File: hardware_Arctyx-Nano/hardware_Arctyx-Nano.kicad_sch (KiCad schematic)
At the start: 54 parts, among them J1 USB_C_Receptacle_USB2.0_16P, J2 Conn_01x20_Pin, J3 Conn_01x20_Pin, SW1 SW_Push, SW2 SW_Push, U1 ICE40UP5K-SG48ITR, U2 RP2350A-QFN60, U3 W25Q128JVS, U4 RT8075ZQW, U5 TJ-S1608SW6TDSLCCYRGB-A5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

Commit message: schematic
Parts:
- added D1, D2, D3, D4: LED, symbol Device:LED
- L2, L3: value L -> 3.3u
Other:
- moved on the sheet: J3

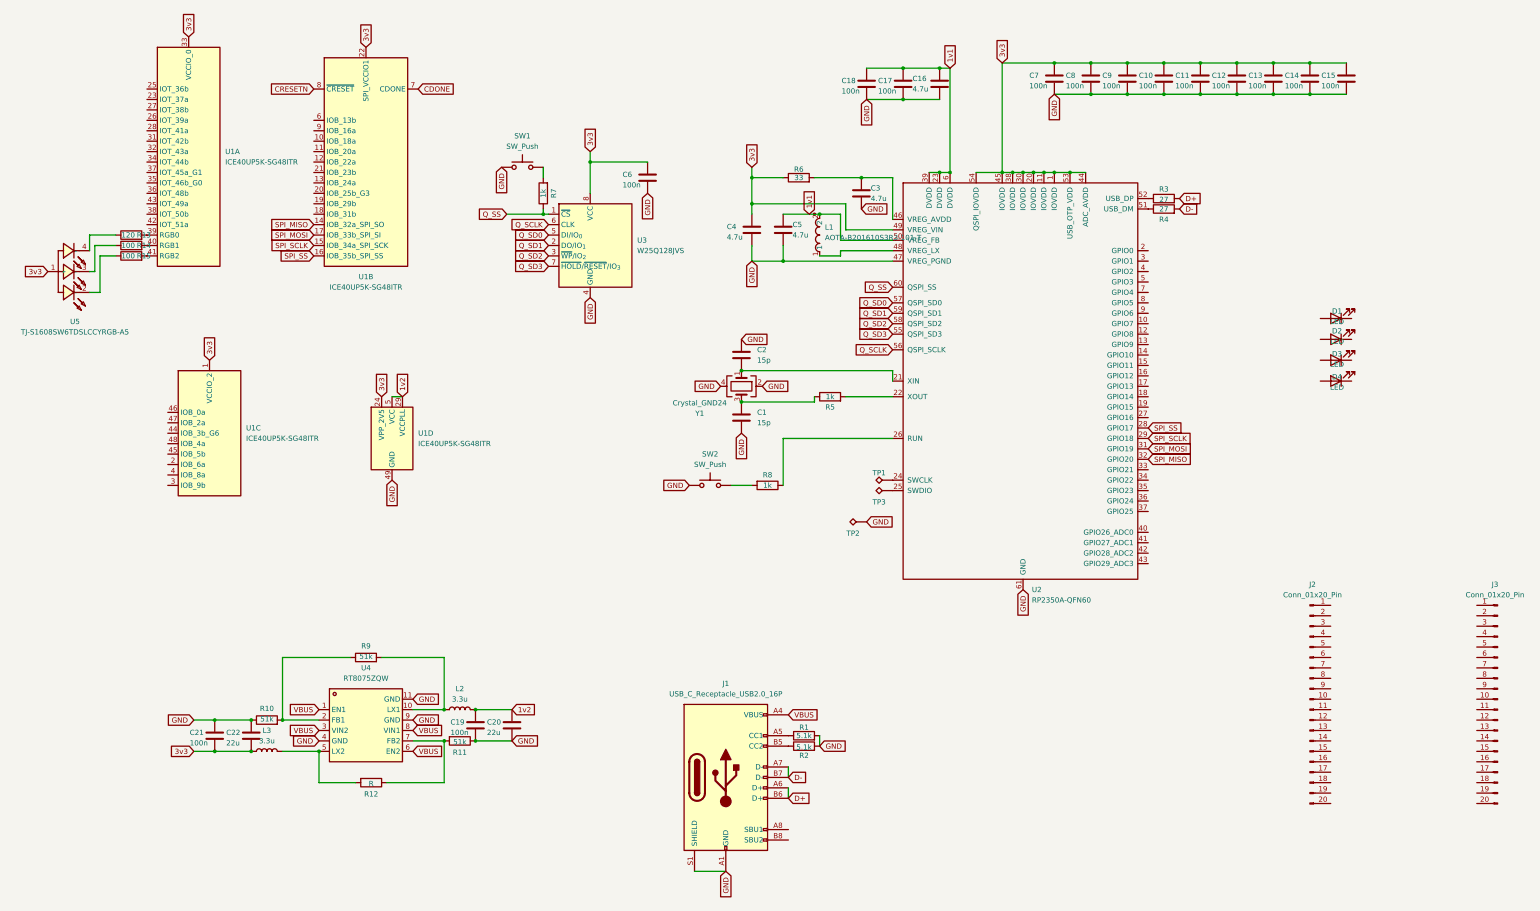
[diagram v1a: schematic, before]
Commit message: Routing the PCB
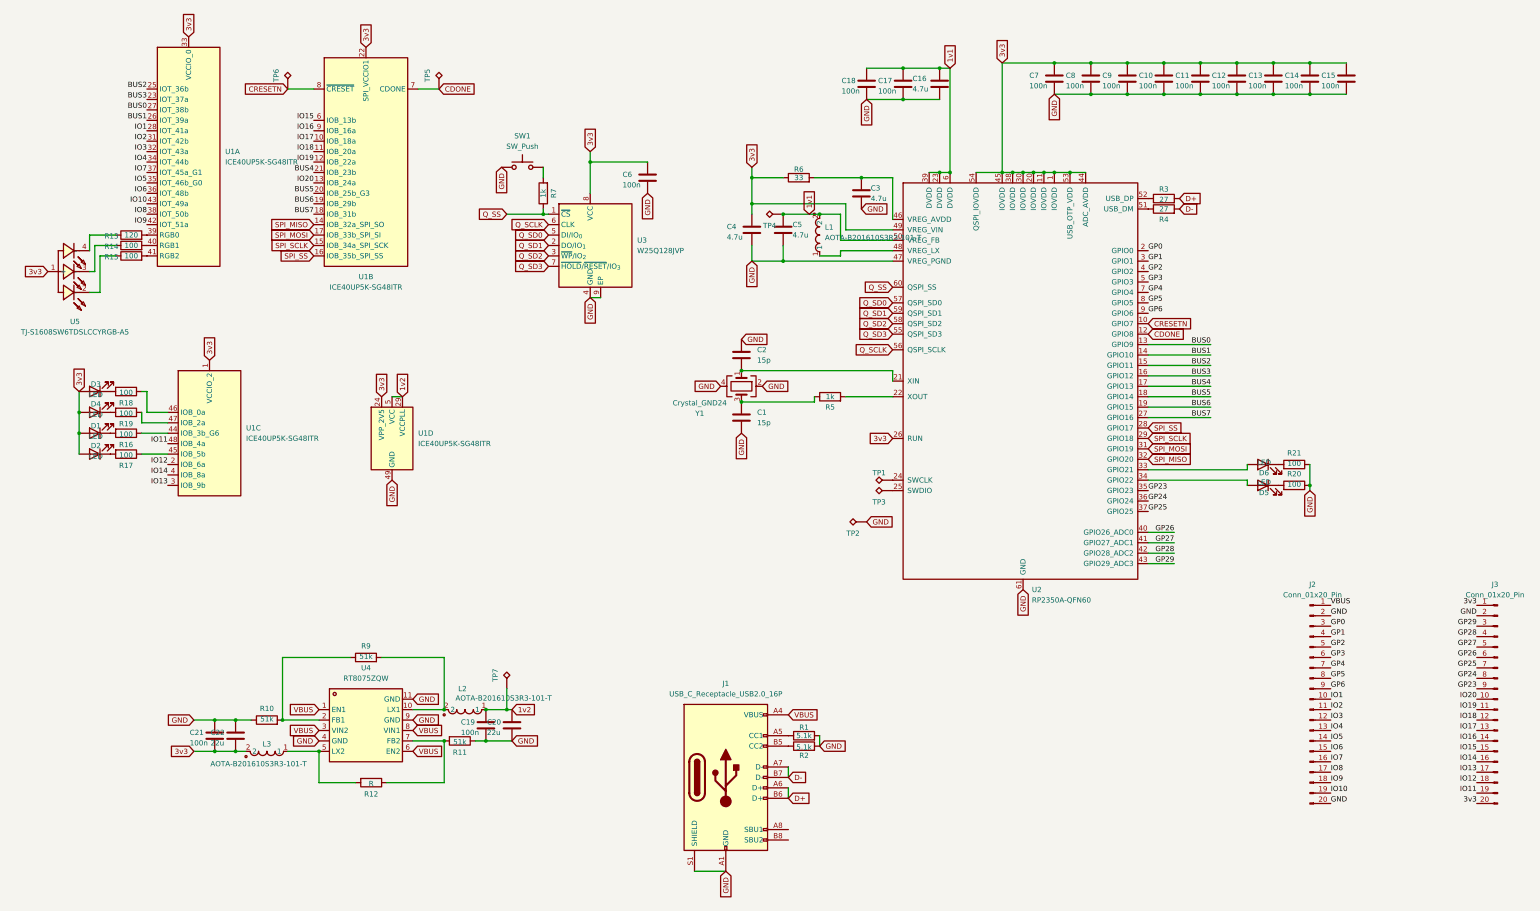
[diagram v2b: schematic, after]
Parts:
- removed L2, L3: 3.3u, easyeda2kicad:IND-SMD_L2.0-W1.6_AOTA-B201610S3R3-101-T, symbol Device:L
- removed R8: 1k, Resistor_SMD:R_0402_1005Metric, symbol Device:R
- removed SW2: SW_Push, Button_Switch_SMD:SW_SPST_PTS810, symbol Switch:SW_Push
- removed U3: W25Q128JVS, Package_SO:SOIC-8_5.3x5.3mm_P1.27mm, symbol Memory_Flash:W25Q128JVS
- added D5, D6: LED, LED_SMD:LED_0402_1005Metric, symbol Device:LED
- added L2, L3: AOTA-B201610S3R3-101-T, easyeda2kicad:IND-SMD_L2.0-W1.6_AOTA-B201610S3R3-101-T, symbol easyeda2kicad:AOTA-B201610S3R3-101-T
- added R16, R17, R18, R19, R20, R21: 100, Resistor_SMD:R_0402_1005Metric, symbol Device:R
- added TP4, TP5, TP6, TP7: TestPoint_Alt, TestPoint:TestPoint_Pad_D1.0mm, symbol Connector:TestPoint_Alt
- added U3: W25Q128JVP, Package_SON:WSON-8-1EP_6x5mm_P1.27mm_EP3.4x4.3mm, symbol Memory_Flash:W25Q128JVP
- D1, D2, D3, D4: footprint (none) -> LED_SMD:LED_0402_1005Metric
- J2, J3: footprint Connector_PinSocket_2.54mm:PinSocket_1x20_P2.54mm_Vertical -> Connector_PinHeader_2.54mm:PinHeader_1x20_P2.54mm_Vertical
- SW1: footprint Button_Switch_SMD:SW_SPST_PTS810 -> easyeda2kicad:SW-SMD_L3.9-W3.0-P4.45
- TP1, TP2, TP3: footprint TestPoint:TestPoint_Pad_D1.5mm -> TestPoint:TestPoint_Pad_D1.0mm
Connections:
- net 1v1: now also TP4.1
- net 1v2: now also L2.1, TP7.1
- net 3v3: now also D1.2 (A), D2.2 (A), D3.2 (A), D4.2 (A), J3.1 (Pin_1), J3.20 (Pin_20), U2.26 (RUN), L3.2, U3.8 (VCC)
- net CDONE: now also U2.12 (GPIO8), TP5.1
- net CRESETN: now also U2.10 (GPIO7), TP6.1
- net GND: now also J2.2 (Pin_2), J2.20 (Pin_20), J3.2 (Pin_2), R20.1, R21.1, U3.4 (GND), U3.9 (EP)
- net Q_SCLK: now also U3.6 (CLK)
- net Q_SD0: now also U3.5 (DI/IO_{0})
- net Q_SD1: now also U3.2 (DO/IO_{1})
- net Q_SD2: now also U3.3 (~{WP}/IO_{2})
- net Q_SD3: now also U3.7 (~{HOLD}/~{RESET}/IO_{3})
- net Q_SS: now also U3.1 (~{CS})
- net VBUS: now also J2.1 (Pin_1)
- net at D4.1 (K): now also R19.2
- net at R9.2, U4.10 (LX1): now also L2.2
- net BUS0: now reaches U2.13 (GPIO9)
- net BUS0: now also U1.27 (IOT_38b)
- net BUS1: now reaches U2.14 (GPIO10)
- net BUS1: now also U1.26 (IOT_39a)
- net BUS2: now reaches U2.15 (GPIO11)
- net BUS2: now also U1.25 (IOT_36b)
- net BUS3: now reaches U2.16 (GPIO12)
- net BUS3: now also U1.23 (IOT_37a)
- net BUS4: now reaches U2.17 (GPIO13)
- net BUS4: now also U1.21 (IOB_23b)
- net BUS5: now reaches U2.18 (GPIO14)
- net BUS5: now also U1.20 (IOB_25b_G3)
- net BUS6: now reaches U2.19 (GPIO15)
- net BUS6: now also U1.19 (IOB_29b)
- net GP0: now reaches U2.2 (GPIO0)
- net GP0: now also J2.3 (Pin_3)
- net BUS7: now reaches U2.27 (GPIO16)
- net BUS7: now also U1.18 (IOB_31b)
- net GP1: now reaches U2.3 (GPIO1)
- net GP1: now also J2.4 (Pin_4)
- net at U2.33 (GPIO21): now also D6.2 (A)
- net at U2.34 (GPIO22): now also D5.2 (A)
- net GP23: now reaches U2.35 (GPIO23)
- net GP23: now also J3.9 (Pin_9)
- net GP24: now reaches U2.36 (GPIO24)
- net GP24: now also J3.8 (Pin_8)
- net GP25: now reaches U2.37 (GPIO25)
- net GP25: now also J3.7 (Pin_7)
- net GP2: now reaches U2.4 (GPIO2)
- net GP2: now also J2.5 (Pin_5)
- net GP26: now reaches U2.40 (GPIO26_ADC0)
- net GP26: now also J3.6 (Pin_6)
- net GP27: now reaches U2.41 (GPIO27_ADC1)
- net GP27: now also J3.5 (Pin_5)
- net GP28: now reaches U2.42 (GPIO28_ADC2)
- net GP28: now also J3.4 (Pin_4)
- net GP29: now reaches U2.43 (GPIO29_ADC3)
- net GP29: now also J3.3 (Pin_3)
- net GP3: now reaches U2.5 (GPIO3)
- net GP3: now also J2.6 (Pin_6)
- net GP4: now reaches U2.7 (GPIO4)
- net GP4: now also J2.7 (Pin_7)
- net GP5: now reaches U2.8 (GPIO5)
- net GP5: now also J2.8 (Pin_8)
- net GP6: now reaches U2.9 (GPIO6)
- net GP6: now also J2.9 (Pin_9)
- net at R12.2, U4.5 (LX2): now also L3.1
- net IO1: now reaches U1.28 (IOT_41a)
- net IO1: now also J2.10 (Pin_10)
- net IO2: now reaches U1.31 (IOT_42b)
- net IO2: now also J2.11 (Pin_11)
- net IO3: now reaches U1.32 (IOT_43a)
- net IO3: now also J2.12 (Pin_12)
- net IO4: now reaches U1.34 (IOT_44b)
- net IO4: now also J2.13 (Pin_13)
- net IO5: now reaches U1.35 (IOT_46b_G0)
- net IO5: now also J2.14 (Pin_14)
- net IO6: now reaches U1.36 (IOT_48b)
- net IO6: now also J2.15 (Pin_15)
- net IO7: now reaches U1.37 (IOT_45a_G1)
- net IO7: now also J2.16 (Pin_16)
- net IO8: now reaches U1.38 (IOT_50b)
- net IO8: now also J2.17 (Pin_17)
- net IO9: now reaches U1.42 (IOT_51a)
- net IO9: now also J2.18 (Pin_18)
- net IO10: now reaches U1.43 (IOT_49a)
- net IO10: now also J2.19 (Pin_19)
- net IO20: now reaches J3.10 (Pin_10)
- net IO20: now also U1.13 (IOB_24a)
- net IO19: now reaches J3.11 (Pin_11)
- net IO19: now also U1.12 (IOB_22a)
- net IO18: now reaches J3.12 (Pin_12)
- net IO18: now also U1.11 (IOB_20a)
- net IO17: now reaches J3.13 (Pin_13)
- net IO17: now also U1.10 (IOB_18a)
- net IO16: now reaches J3.14 (Pin_14)
- net IO16: now also U1.9 (IOB_16a)
- net IO15: now reaches J3.15 (Pin_15)
- net IO15: now also U1.6 (IOB_13b)
- net IO14: now reaches J3.16 (Pin_16)
- net IO14: now also U1.4 (IOB_8a)
- net IO13: now reaches J3.17 (Pin_17)
- net IO13: now also U1.3 (IOB_9b)
- net IO12: now reaches J3.18 (Pin_18)
- net IO12: now also U1.2 (IOB_6a)
- net IO11: now reaches J3.19 (Pin_19)
- net IO11: now also U1.48 (IOB_4a)
- net at D2.1 (K): now also R17.2
- net at D3.1 (K): now also R18.2
- net at D1.1 (K): now also R16.2
- net at U1.44 (IOB_3b_G6): now also R16.1
- net at U1.45 (IOB_5b): now also R17.1
- net at U1.46 (IOB_0a): now also R18.1
- net at U1.47 (IOB_2a): now also R19.1
- new net: D6.1 (K), R21.2
- new net: D5.1 (K), R20.2
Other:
- moved on the sheet: C19, C22, D1, D2

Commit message: PCB Routing
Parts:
- added C23: 4.7u, Capacitor_SMD:C_0402_1005Metric, symbol Device:C
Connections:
- net 1v2: now also C23.1
- net GND: now also C23.2
- net at R17.1: now also U1.46 (IOB_0a); no longer U1.45 (IOB_5b)
- net at R18.1: now also U1.45 (IOB_5b); no longer U1.46 (IOB_0a)
- net at R16.1: now also U1.47 (IOB_2a); no longer U1.44 (IOB_3b_G6)
- net at R19.1: now also U1.44 (IOB_3b_G6); no longer U1.47 (IOB_2a)
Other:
- moved on the sheet: D1, D2, D3, D4, R16, R17, R18, R19

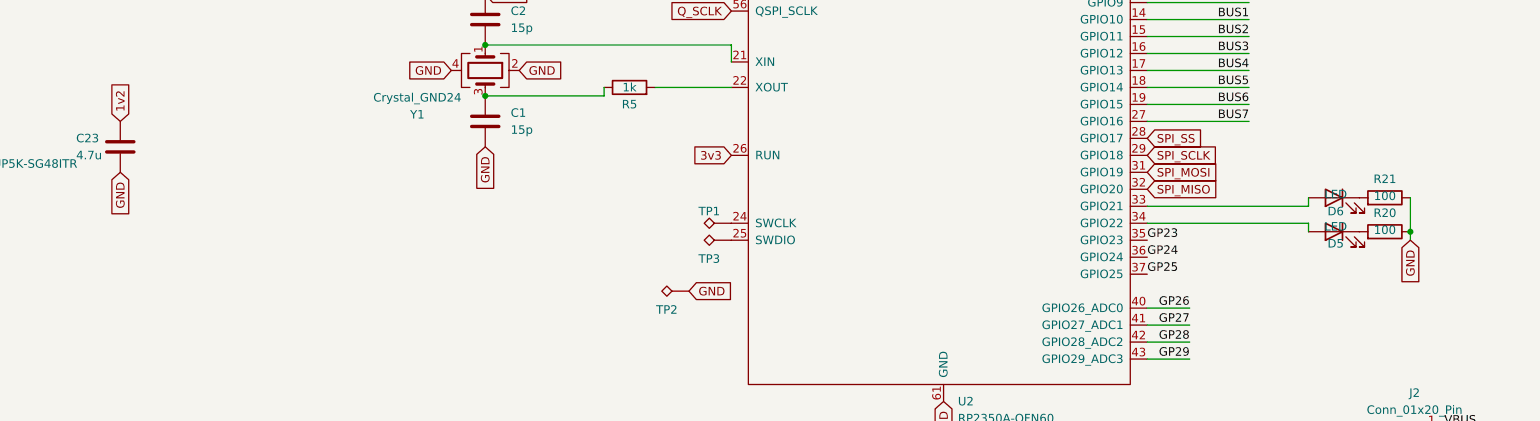
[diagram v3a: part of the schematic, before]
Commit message: PCB fixing errors
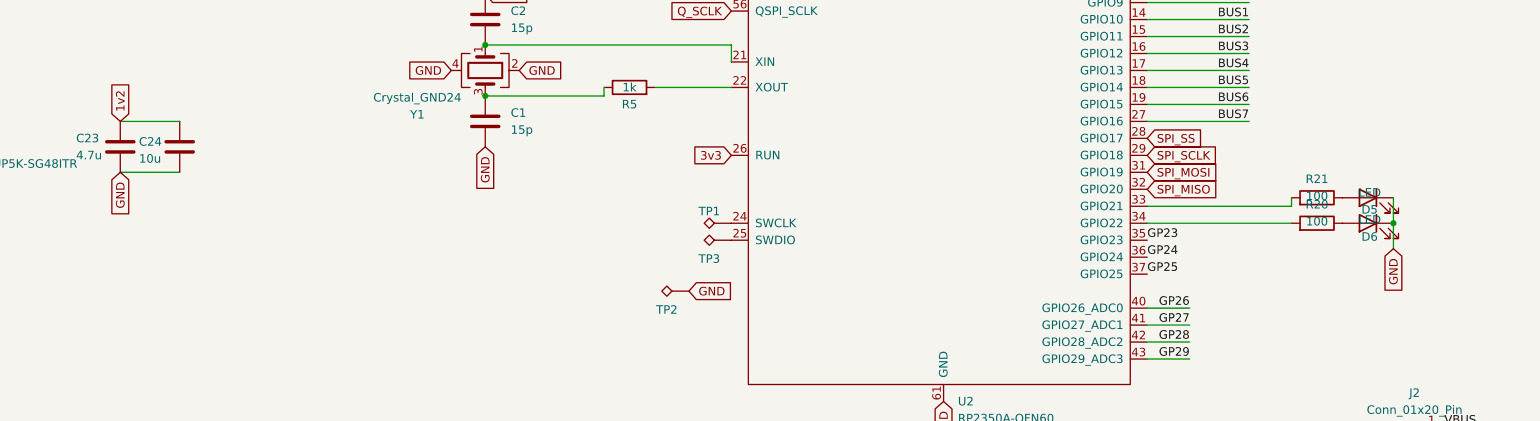
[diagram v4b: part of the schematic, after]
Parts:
- added C24: 10u, Capacitor_SMD:C_0603_1608Metric, symbol Device:C
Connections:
- net 1v2: now also C24.1
- net GND: now also D5.1 (K), D6.1 (K), C24.2; no longer R20.1, R21.1
- net at U2.33 (GPIO21): now also R21.2; no longer D6.2 (A)
- net at U2.34 (GPIO22): now also R20.2; no longer D5.2 (A)
- new net: D6.2 (A), R20.1
- new net: D5.2 (A), R21.1
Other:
- moved on the sheet: D5, D6, R20, R21
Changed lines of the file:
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@@
 	)
 	(junction
+		(at 330.2 156.21)
+		(diameter 0)
+		(color 0 0 0 0)
+	)
+	(junction
 		(at 288.29 54.61)
 		(diameter 0)
@@
 	)
 	(junction
-		(at 332.74 157.48)
-		(diameter 0)
-		(color 0 0 0 0)
-	)
-	(junction
 		(at 91.44 222.25)
 		(diameter 0)
@@
 	(wire
 		(pts
+			(xy 330.2 152.4) (xy 330.2 156.21)
+		)
+		(stroke
+			(width 0)
+			(type default)
+		)
+	)
+	(wire
+		(pts
 			(xy 196.85 88.9) (xy 196.85 82.55)
 		)
@@
 	(wire
 		(pts
-			(xy 317.5 152.4) (xy 317.5 153.67)
+			(xy 314.96 153.67) (xy 314.96 152.4)
 		)
 		(stroke
@@
 	(wire
 		(pts
-			(xy 332.74 157.48) (xy 332.74 158.75)
-		)
-		(stroke
-			(width 0)
-			(type default)
-		)
-	)
-	(wire
-		(pts
-			(xy 317.5 156.21) (xy 317.5 157.48)
+			(xy 139.7 140.97) (xy 148.59 140.97)
 		)
 		(stroke
@@
 	(wire
 		(pts
-			(xy 293.37 156.21) (xy 317.5 156.21)
+			(xy 293.37 156.21) (xy 314.96 156.21)
 		)
 		(stroke
@@
 	(wire
 		(pts
-			(xy 332.74 152.4) (xy 332.74 157.48)
+			(xy 204.47 102.87) (xy 231.14 102.87)
 		)
 		(stroke
@@
 	(wire
 		(pts
-			(xy 204.47 102.87) (xy 231.14 102.87)
+			(xy 196.85 82.55) (xy 204.47 82.55)
 		)
 		(stroke
@@
 	(wire
 		(pts
-			(xy 196.85 82.55) (xy 204.47 82.55)
+			(xy 279.4 62.23) (xy 288.29 62.23)
 		)
 		(stroke
@@
 	(wire
 		(pts
-			(xy 279.4 62.23) (xy 288.29 62.23)
+			(xy 132.08 212.09) (xy 137.16 212.09)
 		)
 		(stroke
@@
 	(wire
 		(pts
-			(xy 132.08 212.09) (xy 137.16 212.09)
+			(xy 139.7 148.59) (xy 148.59 148.59)
 		)
 		(stroke
@@
 	(wire
 		(pts
-			(xy 138.43 219.71) (xy 132.08 219.71)
+			(xy 330.2 156.21) (xy 330.2 160.02)
 		)
 		(stroke
@@
 	(wire
 		(pts
-			(xy 66.04 214.63) (xy 71.12 214.63)
+			(xy 138.43 219.71) (xy 132.08 219.71)
 		)
 		(stroke
@@
 	(wire
 		(pts
-			(xy 213.36 218.44) (xy 213.36 220.98)
+			(xy 66.04 214.63) (xy 71.12 214.63)
 		)
 		(stroke
@@
 	(wire
 		(pts
-			(xy 293.37 171.45) (xy 299.72 171.45)
+			(xy 213.36 218.44) (xy 213.36 220.98)
 		)
 		(stroke
@@
 	(wire
 		(pts
-			(xy 196.85 99.06) (xy 196.85 102.87)
+			(xy 293.37 171.45) (xy 299.72 171.45)
 		)
 		(stroke
@@
 	(wire
 		(pts
-			(xy 121.92 199.39) (xy 121.92 212.09)
+			(xy 196.85 99.06) (xy 196.85 102.87)
 		)
 		(stroke
@@
 	(wire
 		(pts
-			(xy 308.61 133.35) (xy 293.37 133.35)
+			(xy 121.92 199.39) (xy 121.92 212.09)
 		)
 		(stroke
@@
 	(wire
 		(pts
-			(xy 317.5 153.67) (xy 293.37 153.67)
+			(xy 308.61 133.35) (xy 293.37 133.35)
 		)
 		(stroke
@@
 	(wire
 		(pts
+			(xy 293.37 153.67) (xy 314.96 153.67)
+		)
+		(stroke
+			(width 0)
+			(type default)
+		)
+	)
+	(wire
+		(pts
 			(xy 194.31 137.16) (xy 212.09 137.16)
 		)
@@
 	(global_label "GND"
 		(shape input)
-		(at 332.74 158.75 270)
+		(at 330.2 160.02 270)
 		(fields_autoplaced yes)
 		(effects
@@
 		)
 		(property "Intersheetrefs" "${INTERSHEET_REFS}"
-			(at 332.74 165.6057 90)
+			(at 330.2 166.8757 90)
 			(effects
 				(font
@@
 	(symbol
 		(lib_id "Device:LED")
-		(at 321.31 152.4 0)
+		(at 326.39 156.21 0)
 		(mirror y)
 		(unit 1)
@@
 		(dnp no)
 		(property "Reference" "D6"
-			(at 321.564 154.432 0)
+			(at 326.644 158.242 0)
 			(effects
 				(font
@@
 		)
 		(property "Value" "LED"
-			(at 321.564 151.892 0)
+			(at 326.644 155.702 0)
 			(effects
 				(font
@@
 		)
 		(property "Footprint" "LED_SMD:LED_0402_1005Metric"
-			(at 321.31 152.4 0)
+			(at 326.39 156.21 0)
 			(effects
 				(font
@@
 		)
 		(property "Datasheet" "~"
-			(at 321.31 152.4 0)
+			(at 326.39 156.21 0)
 			(effects
 				(font
@@
 		)
 		(property "Description" "Light emitting diode"
-			(at 321.31 152.4 0)
+			(at 326.39 156.21 0)
 			(effects
 				(font
@@
 		)
 		(property "Sim.Pins" "1=K 2=A"
-			(at 321.31 152.4 0)
+			(at 326.39 156.21 0)
 			(effects
 				(font
@@
 	(symbol
 		(lib_id "Device:C")
+		(at 148.59 144.78 0)
+		(unit 1)
+		(exclude_from_sim no)
+		(in_bom yes)
+		(on_board yes)
+		(dnp no)
+		(property "Reference" "C24"
+			(at 142.494 144.018 0)
+			(effects
+				(font
+					(size 1.27 1.27)
+				)
+				(justify left)
+			)
+		)
+		(property "Value" "10u"
+			(at 142.494 146.558 0)
+			(effects
+				(font
+					(size 1.27 1.27)
+				)
+				(justify left)
+			)
+		)
+		(property "Footprint" "Capacitor_SMD:C_0603_1608Metric"
+			(at 149.5552 148.59 0)
+			(effects
+				(font
+					(size 1.27 1.27)
+				)
+				(hide yes)
+			)
+		)
+		(property "Datasheet" "~"
+			(at 148.59 144.78 0)
+			(effects
+				(font
+					(size 1.27 1.27)
+				)
+				(hide yes)
+			)
+		)
+		(property "Description" "Unpolarized capacitor"
+			(at 148.59 144.78 0)
+			(effects
+				(font
+					(size 1.27 1.27)
+				)
+				(hide yes)
+			)
+		)
+		(pin "1"
+		)
+		(pin "2"
+		)
+		(instances
+			(project "hardware_Arctyx-Nano"
+				(path "/dadf11aa-8e96-42b0-bb48-2980919511bd"
+					(reference "C24")
+					(unit 1)
+				)
+			)
+		)
+	)
+	(symbol
+		(lib_id "Device:C")
 		(at 139.7 144.78 0)
 		(unit 1)
@@
 	(symbol
 		(lib_id "Device:LED")
-		(at 321.31 157.48 0)
+		(at 326.39 152.4 0)
 		(mirror y)
 		(unit 1)
@@
 		(dnp no)
 		(property "Reference" "D5"
-			(at 321.564 159.258 0)
+			(at 326.644 154.178 0)
 			(effects
 				(font
@@
 		)
 		(property "Value" "LED"
-			(at 321.564 156.718 0)
+			(at 326.644 151.638 0)
 			(effects
 				(font
@@
 		)
 		(property "Footprint" "LED_SMD:LED_0402_1005Metric"
-			(at 321.31 157.48 0)
+			(at 326.39 152.4 0)
 			(effects
 				(font
@@
 		)
 		(property "Datasheet" "~"
-			(at 321.31 157.48 0)
+			(at 326.39 152.4 0)
 			(effects
 				(font
@@
 		)
 		(property "Description" "Light emitting diode"
-			(at 321.31 157.48 0)
+			(at 326.39 152.4 0)
 			(effects
 				(font
@@
 		)
 		(property "Sim.Pins" "1=K 2=A"
-			(at 321.31 157.48 0)
+			(at 326.39 152.4 0)
 			(effects
 				(font
@@
 	(symbol
 		(lib_id "Device:R")
-		(at 328.93 157.48 270)
+		(at 318.77 156.21 270)
 		(mirror x)
 		(unit 1)
@@
 		(dnp no)
 		(property "Reference" "R20"
-			(at 328.93 154.686 90)
+			(at 318.77 153.416 90)
 			(effects
 				(font
@@
 		)
 		(property "Value" "100"
-			(at 328.93 157.226 90)
+			(at 318.77 155.956 90)
 			(effects
 				(font
@@
 		)
 		(property "Footprint" "Resistor_SMD:R_0402_1005Metric"
-			(at 328.93 159.258 90)
+			(at 318.77 157.988 90)
 			(effects
 				(font
@@
 		)
 		(property "Datasheet" "~"
-			(at 328.93 157.48 0)
+			(at 318.77 156.21 0)
 			(effects
 				(font
@@
 		)
 		(property "Description" "Resistor"
-			(at 328.93 157.48 0)
+			(at 318.77 156.21 0)
 			(effects
 				(font
@@
 	(symbol
 		(lib_id "Device:R")
-		(at 328.93 152.4 270)
+		(at 318.77 152.4 270)
 		(mirror x)
 		(unit 1)
@@
 		(dnp no)
 		(property "Reference" "R21"
-			(at 328.93 149.606 90)
+			(at 318.77 149.606 90)
 			(effects
 				(font
@@
 		)
 		(property "Value" "100"
-			(at 328.93 152.146 90)
+			(at 318.77 152.146 90)
 			(effects
 				(font
@@
 		)
 		(property "Footprint" "Resistor_SMD:R_0402_1005Metric"
-			(at 328.93 154.178 90)
+			(at 318.77 154.178 90)
 			(effects
 				(font
@@
 		)
 		(property "Datasheet" "~"
-			(at 328.93 152.4 0)
+			(at 318.77 152.4 0)
 			(effects
 				(font
@@
 		)
 		(property "Description" "Resistor"
-			(at 328.93 152.4 0)
+			(at 318.77 152.4 0)
 			(effects
 				(font
